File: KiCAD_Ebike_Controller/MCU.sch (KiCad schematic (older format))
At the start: 16 parts, among them SW1 SW_Push, U1 STM32F030K6Tx, Y1 Crystal_GND2_Small

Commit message: 50% of the way through the layout
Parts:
- removed R20: 100k, symbol Device:R_Small
- removed Y1: Crystal_GND2_Small, symbol Device:Crystal_GND2_Small
- added C33, C34: 100n, Capacitor_SMD:C_0805_2012Metric_Pad1.15x1.40mm_HandSolder, symbol Device:C_Small
- added Y1: Crystal, Crystal:Crystal_SMD_HC49-SD, symbol Device:Crystal
- C5: value 10n -> 100n; footprint Capacitor_SMD:C_0603_1608Metric_Pad1.05x0.95mm_HandSolder -> Capacitor_SMD:C_0805_2012Metric_Pad1.15x1.40mm_HandSolder
- C6, C7, C8: footprint Capacitor_SMD:C_0805_2012Metric -> Capacitor_SMD:C_0805_2012Metric_Pad1.15x1.40mm_HandSolder
- R16, R17, R18, R19: footprint (none) -> Resistor_SMD:R_0805_2012Metric_Pad1.15x1.40mm_HandSolder
- SW1: footprint (none) -> Button_Switch_SMD:SW_Push_1P1T_NO_6x6mm_H9.5mm
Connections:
- net labels added: GNDA
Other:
- moved on the sheet: C8
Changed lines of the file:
@@
 SPI1_NSS
-$Comp
-L Device:Crystal_GND2_Small Y1
-U 1 1 5F915CDC
-P 4800 3650
-F 0 "Y1" V 4800 3750 50  0000 L CNN
-F 1 "Crystal_GND2_Small" V 4800 2650 50  0001 L CNN
-F 2 "" H 4800 3650 50  0001 C CNN
-F 3 "~" H 4800 3650 50  0001 C CNN
-	1    4800 3650
-	0    1    1    0
-$EndComp
 $Comp
 L Device:C_Small C11
@@
 $EndComp
 Wire Wire Line
-	4800 3550 4800 3500
-Wire Wire Line
-	4800 3500 4650 3500
-Wire Wire Line
-	4800 3750 4800 3800
-Wire Wire Line
-	4800 3800 4650 3800
-Wire Wire Line
-	4400 3800 4400 3650
-Wire Wire Line
 	4400 3500 4450 3500
 Wire Wire Line
-	4700 3650 4400 3650
-Connection ~ 4400 3650
-Wire Wire Line
-	4400 3650 4400 3500
-Wire Wire Line
-	5000 3500 4800 3500
-Wire Wire Line
 	5000 3500 5000 3600
-Connection ~ 4800 3500
-Wire Wire Line
-	4800 3800 5000 3800
 Wire Wire Line
 	5000 3700 5000 3800
-Connection ~ 4800 3800
 $Comp
 L Device:C_Small C10
@@
 	7850 4500 6100 4500
 Wire Wire Line
-	5000 4100 3450 4100
+	5000 4100 3400 4100
 Text HLabel 2550 3900 0    50   Input ~ 0
 HALL_A_PB0
@@
 Wire Wire Line
 	6100 4400 7850 4400
-Wire Wire Line
-	5000 3000 4650 3000
 Text HLabel 2550 3000 0    50   Input ~ 0
 nRST
-$Comp
-L Device:R_Small R20
-U 1 1 5F9AB9AE
-P 4650 2850
-F 0 "R20" H 4709 2896 50  0000 L CNN
-F 1 "100k" H 4709 2805 50  0000 L CNN
-F 2 "" H 4650 2850 50  0001 C CNN
-F 3 "~" H 4650 2850 50  0001 C CNN
-	1    4650 2850
-	1    0    0    -1
-$EndComp
 Connection ~ 3950 3000
 Wire Wire Line
 	3950 3000 3950 3100
-Wire Wire Line
-	4650 2750 4650 2700
-Wire Wire Line
-	4650 2700 5500 2700
-Connection ~ 5500 2700
 $Comp
 L Device:C_Small C9
@@
 Wire Wire Line
 	3950 3000 3700 3000
-Wire Wire Line
-	4650 2950 4650 3000
-Connection ~ 4650 3000
-Wire Wire Line
-	4650 3000 3950 3000
 $Comp
 L Switch:SW_Push SW1
@@
 F 0 "SW1" V 3654 3202 50  0000 R CNN
 F 1 "SW_Push" V 3745 3202 50  0000 R CNN
-F 2 "" H 3700 3450 50  0001 C CNN
+F 2 "Button_Switch_SMD:SW_Push_1P1T_NO_6x6mm_H9.5mm" H 3700 3450 50  0001 C CNN
 F 3 "~" H 3700 3450 50  0001 C CNN
 	1    3700 3250
@@
 F 0 "R19" H 4359 3346 50  0000 L CNN
 F 1 "100k" H 4359 3255 50  0000 L CNN
-F 2 "" H 4300 3300 50  0001 C CNN
+F 2 "Resistor_SMD:R_0805_2012Metric_Pad1.15x1.40mm_HandSolder" H 4300 3300 50  0001 C CNN
 F 3 "~" H 4300 3300 50  0001 C CNN
 	1    4300 3300
@@
 F 0 "R16" H 2759 3746 50  0000 L CNN
 F 1 "100k" H 2759 3655 50  0000 L CNN
-F 2 "" H 2700 3700 50  0001 C CNN
+F 2 "Resistor_SMD:R_0805_2012Metric_Pad1.15x1.40mm_HandSolder" H 2700 3700 50  0001 C CNN
 F 3 "~" H 2700 3700 50  0001 C CNN
 	1    2700 3700
@@
 F 0 "R17" H 3059 3746 50  0000 L CNN
 F 1 "100k" H 3059 3655 50  0000 L CNN
-F 2 "" H 3000 3700 50  0001 C CNN
+F 2 "Resistor_SMD:R_0805_2012Metric_Pad1.15x1.40mm_HandSolder" H 3000 3700 50  0001 C CNN
 F 3 "~" H 3000 3700 50  0001 C CNN
 	1    3000 3700
@@
 F 0 "R18" H 3359 3746 50  0000 L CNN
 F 1 "100k" H 3359 3655 50  0000 L CNN
-F 2 "" H 3300 3700 50  0001 C CNN
+F 2 "Resistor_SMD:R_0805_2012Metric_Pad1.15x1.40mm_HandSolder" H 3300 3700 50  0001 C CNN
 F 3 "~" H 3300 3700 50  0001 C CNN
 	1    3300 3700
@@
 Text HLabel 1600 1950 0    50   Input ~ 0
 +3.3v
-$Comp
-L power:GND #PWR0110
-U 1 1 5FABED44
-P 1950 2600
-F 0 "#PWR0110" H 1950 2350 50  0001 C CNN
-F 1 "GND" H 1955 2427 50  0000 C CNN
-F 2 "" H 1950 2600 50  0001 C CNN
-F 3 "" H 1950 2600 50  0001 C CNN
-	1    1950 2600
-	1    0    0    -1
-$EndComp
-$Comp
-L power:GND #PWR0111
-U 1 1 5FACF53C
-P 3700 3650
-F 0 "#PWR0111" H 3700 3400 50  0001 C CNN
-F 1 "GND" H 3705 3477 50  0000 C CNN
-F 2 "" H 3700 3650 50  0001 C CNN
-F 3 "" H 3700 3650 50  0001 C CNN
-	1    3700 3650
-	1    0    0    -1
-$EndComp
-$Comp
-L power:GND #PWR0112
-U 1 1 5FACFE3C
-P 5500 4950
-F 0 "#PWR0112" H 5500 4700 50  0001 C CNN
-F 1 "GND" H 5505 4777 50  0000 C CNN
-F 2 "" H 5500 4950 50  0001 C CNN
-F 3 "" H 5500 4950 50  0001 C CNN
-	1    5500 4950
-	1    0    0    -1
-$EndComp
 Wire Wire Line
 	1600 2300 1950 2300
@@
 Text Notes 6200 3200 0    50   ~ 0
 ADC_IN2
-Text HLabel 7850 3200 2    50   Input ~ 0
-THROTTLE_PA2
-Wire Wire Line
-	6100 3200 7850 3200
 Wire Wire Line
 	7100 3800 7100 3850
@@
 F 0 "C6" H 2892 4796 50  0000 L CNN
 F 1 "100n" H 2892 4705 50  0000 L CNN
-F 2 "Capacitor_SMD:C_0805_2012Metric" H 2800 4750 50  0001 C CNN
+F 2 "Capacitor_SMD:C_0805_2012Metric_Pad1.15x1.40mm_HandSolder" H 2800 4750 50  0001 C CNN
 F 3 "~" H 2800 4750 50  0001 C CNN
 	1    2800 4750
@@
 F 0 "C7" H 3192 4796 50  0000 L CNN
 F 1 "100n" H 3192 4705 50  0000 L CNN
-F 2 "Capacitor_SMD:C_0805_2012Metric" H 3100 4750 50  0001 C CNN
+F 2 "Capacitor_SMD:C_0805_2012Metric_Pad1.15x1.40mm_HandSolder" H 3100 4750 50  0001 C CNN
 F 3 "~" H 3100 4750 50  0001 C CNN
 	1    3100 4750
@@
 L Device:C_Small C8
 U 1 1 5FCC70C3
-P 3450 4750
-F 0 "C8" H 3542 4796 50  0000 L CNN
-F 1 "100n" H 3542 4705 50  0000 L CNN
-F 2 "Capacitor_SMD:C_0805_2012Metric" H 3450 4750 50  0001 C CNN
-F 3 "~" H 3450 4750 50  0001 C CNN
-	1    3450 4750
+P 3400 4750
+F 0 "C8" H 3492 4796 50  0000 L CNN
+F 1 "100n" H 3492 4705 50  0000 L CNN
+F 2 "Capacitor_SMD:C_0805_2012Metric_Pad1.15x1.40mm_HandSolder" H 3400 4750 50  0001 C CNN
+F 3 "~" H 3400 4750 50  0001 C CNN
+	1    3400 4750
 	1    0    0    -1
 $EndComp
@@
 	3100 4000 5000 4000
 Wire Wire Line
-	3450 4100 3450 4650
-Connection ~ 3450 4100
-Wire Wire Line
-	3450 4100 3300 4100
+	3400 4100 3400 4650
+Connection ~ 3400 4100
+Wire Wire Line
+	3400 4100 3300 4100
 Wire Wire Line
 	2800 4850 2800 5000
@@
 	2800 5000 3100 5000
 Wire Wire Line
-	3450 5000 3450 4850
+	3400 5000 3400 4850
 Wire Wire Line
 	3100 4850 3100 5000
 Connection ~ 3100 5000
-$Comp
-L power:GND #PWR0113
-U 1 1 5FCE6083
-P 3200 5150
-F 0 "#PWR0113" H 3200 4900 50  0001 C CNN
-F 1 "GND" H 3205 4977 50  0000 C CNN
-F 2 "" H 3200 5150 50  0001 C CNN
-F 3 "" H 3200 5150 50  0001 C CNN
-	1    3200 5150
-	1    0    0    -1
-$EndComp
 Wire Wire Line
 	3100 5000 3200 5000
@@
 Connection ~ 3200 5000
 Wire Wire Line
-	3200 5000 3450 5000
+	3200 5000 3400 5000
 $Comp
 L Device:C_Small C5
@@
 P 2450 2150
 F 0 "C5" H 2542 2196 50  0000 L CNN
-F 1 "10n" H 2542 2105 50  0000 L CNN
-F 2 "Capacitor_SMD:C_0603_1608Metric_Pad1.05x0.95mm_HandSolder" H 2450 2150 50  0001 C CNN
+F 1 "100n" H 2542 2105 50  0000 L CNN
+F 2 "Capacitor_SMD:C_0805_2012Metric_Pad1.15x1.40mm_HandSolder" H 2450 2150 50  0001 C CNN
 F 3 "~" H 2450 2150 50  0001 C CNN
 	1    2450 2150
@@
 Wire Wire Line
 	2450 2300 2100 2300
+Connection ~ 2100 2300
+Wire Wire Line
+	3950 3000 5000 3000
+$Comp
+L power:GNDA #PWR0113
+U 1 1 5FEA90DB
+P 5500 4950
+F 0 "#PWR0113" H 5500 4700 50  0001 C CNN
+F 1 "GNDA" H 5505 4777 50  0000 C CNN
+F 2 "" H 5500 4950 50  0001 C CNN
+F 3 "" H 5500 4950 50  0001 C CNN
+	1    5500 4950
+	1    0    0    -1
+$EndComp
+$Comp
+L power:GNDA #PWR0116
+U 1 1 5FEAA964
+P 3700 3650
+F 0 "#PWR0116" H 3700 3400 50  0001 C CNN
+F 1 "GNDA" H 3705 3477 50  0000 C CNN
+F 2 "" H 3700 3650 50  0001 C CNN
+F 3 "" H 3700 3650 50  0001 C CNN
+	1    3700 3650
+	1    0    0    -1
+$EndComp
+$Comp
+L power:GNDA #PWR0122
+U 1 1 5FEAF53C
+P 3200 5150
+F 0 "#PWR0122" H 3200 4900 50  0001 C CNN
+F 1 "GNDA" H 3205 4977 50  0000 C CNN
+F 2 "" H 3200 5150 50  0001 C CNN
+F 3 "" H 3200 5150 50  0001 C CNN
+	1    3200 5150
+	1    0    0    -1
+$EndComp
+$Comp
+L power:GNDA #PWR0123
+U 1 1 5FEB4CC6
+P 1950 2600
+F 0 "#PWR0123" H 1950 2350 50  0001 C CNN
+F 1 "GNDA" H 1955 2427 50  0000 C CNN
+F 2 "" H 1950 2600 50  0001 C CNN
+F 3 "" H 1950 2600 50  0001 C CNN
+	1    1950 2600
+	1    0    0    -1
+$EndComp
+Wire Wire Line
+	4400 3500 4400 3800
+Wire Wire Line
+	5000 3500 4800 3500
+Connection ~ 4800 3500
+Wire Wire Line
+	4650 3500 4800 3500
+Connection ~ 4800 3800
+Wire Wire Line
+	4800 3800 5000 3800
+Wire Wire Line
+	4650 3800 4800 3800
+$Comp
+L Device:Crystal Y1
+U 1 1 5FF5B830
+P 4800 3650
+F 0 "Y1" V 4600 3650 50  0000 L CNN
+F 1 "Crystal" V 4500 3650 50  0000 L CNN
+F 2 "Crystal:Crystal_SMD_HC49-SD" H 4800 3650 50  0001 C CNN
+F 3 "~" H 4800 3650 50  0001 C CNN
+	1    4800 3650
+	0    1    1    0
+$EndComp
+Text HLabel 7850 3200 2    50   Input ~ 0
+THROTTLE_PA2
+Wire Wire Line
+	6100 3200 7850 3200
+$Comp
+L Device:C_Small C33
+U 1 1 60096170
+P 2850 2150
+F 0 "C33" H 2942 2196 50  0000 L CNN
+F 1 "100n" H 2942 2105 50  0000 L CNN
+F 2 "Capacitor_SMD:C_0805_2012Metric_Pad1.15x1.40mm_HandSolder" H 2850 2150 50  0001 C CNN
+F 3 "~" H 2850 2150 50  0001 C CNN
+	1    2850 2150
+	1    0    0    -1
+$EndComp
+Wire Wire Line
+	2450 1950 2850 1950
+Wire Wire Line
+	2850 1950 2850 2050
+Connection ~ 2450 1950
+Wire Wire Line
+	2850 2250 2850 2300
+Wire Wire Line
+	2850 2300 2450 2300
+Connection ~ 2450 2300
+$Comp
+L Device:C_Small C34
+U 1 1 6009E0FA
+P 3250 2150
+F 0 "C34" H 3342 2196 50  0000 L CNN
+F 1 "100n" H 3342 2105 50  0000 L CNN
+F 2 "Capacitor_SMD:C_0805_2012Metric_Pad1.15x1.40mm_HandSolder" H 3250 2150 50  0001 C CNN
+F 3 "~" H 3250 2150 50  0001 C CNN
+	1    3250 2150
+	1    0    0    -1
+$EndComp
+Wire Wire Line
+	2850 1950 3250 1950
+Wire Wire Line
+	3250 1950 3250 2050
+Connection ~ 2850 1950
+Wire Wire Line
+	3250 2250 3250 2300
+Wire Wire Line
+	3250 2300 2850 2300
+Connection ~ 2850 2300
 Wire Bus Line
 	7200 3900 7200 4100
 Wire Bus Line
 	7150 3500 7150 3800
-Connection ~ 2100 2300
 $EndSCHEMATC

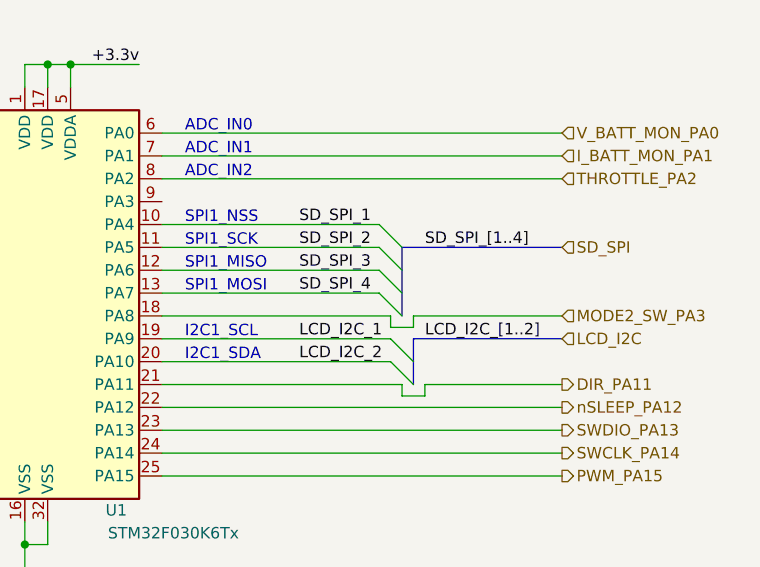
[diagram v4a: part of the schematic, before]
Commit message: Layout done. will tidy up ref des next
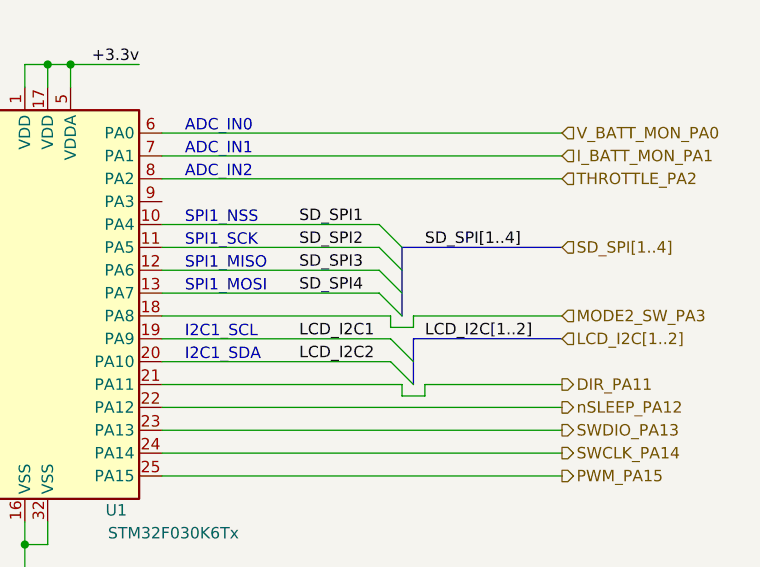
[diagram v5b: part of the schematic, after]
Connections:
- net LCD_I2C_1 renamed LCD_I2C1
- net LCD_I2C_2 renamed LCD_I2C2
- net SD_SPI_1 renamed SD_SPI1
- net SD_SPI_2 renamed SD_SPI2
- net SD_SPI_3 renamed SD_SPI3
- net SD_SPI_4 renamed SD_SPI4
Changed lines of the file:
@@
 $Descr A4 11693 8268
 encoding utf-8
-Sheet 3 7
+Sheet 7 7
 Title ""
 Date ""
@@
 Text HLabel 1600 2300 0    50   Input ~ 0
 GND
-Text HLabel 7850 4500 2    50   Output ~ 0
-PWM_PA15
-Text HLabel 7850 4100 2    50   Output ~ 0
-DIR_PA11
-Text HLabel 7850 4200 2    50   Output ~ 0
-nSLEEP_PA12
 Wire Wire Line
 	6100 3000 7850 3000
@@
 Text Notes 6200 3900 0    50   ~ 0
 I2C1_SCL
-Wire Wire Line
-	7050 3700 6100 3700
 Wire Wire Line
 	6100 3600 7050 3600
@@
 MODE2_SW_PA3
 Text HLabel 7850 3500 2    50   Input ~ 0
-SD_SPI
-Text HLabel 7850 3900 2    50   Input ~ 0
-LCD_I2C
+SD_SPI[1..4]
 Wire Bus Line
 	7150 3500 7850 3500
@@
 	7050 3700 7150 3800
 Text Label 6700 3400 0    50   ~ 0
-SD_SPI_1
+SD_SPI1
 Text Label 6700 3500 0    50   ~ 0
-SD_SPI_2
+SD_SPI2
 Text Label 6700 3600 0    50   ~ 0
-SD_SPI_3
+SD_SPI3
 Text Label 6700 3700 0    50   ~ 0
-SD_SPI_4
+SD_SPI4
 Text Label 7250 3500 0    50   ~ 0
-SD_SPI_[1..4]
+SD_SPI[1..4]
 Text Label 6700 3900 0    50   ~ 0
-LCD_I2C_1
+LCD_I2C1
 Text Label 6700 4000 0    50   ~ 0
-LCD_I2C_2
+LCD_I2C2
 Wire Bus Line
 	7850 3900 7200 3900
 Entry Wire Line
-	7100 4000 7200 4100
-Wire Wire Line
-	6100 4000 7100 4000
-Entry Wire Line
 	7100 3900 7200 4000
 Wire Wire Line
 	6100 3900 7100 3900
-Wire Wire Line
-	7250 4150 7250 4100
-Wire Wire Line
-	7250 4100 7850 4100
-Wire Wire Line
-	7850 4200 6100 4200
-Wire Wire Line
-	7250 4150 7150 4150
-Wire Wire Line
-	7150 4150 7150 4100
-Wire Wire Line
-	7150 4100 6100 4100
 Text Label 7250 3900 0    50   ~ 0
-LCD_I2C_[1..2]
-Wire Wire Line
-	7850 4500 6100 4500
+LCD_I2C[1..2]
 Wire Wire Line
 	5000 4100 3400 4100
@@
 Wire Wire Line
 	5000 4200 2550 4200
-Wire Wire Line
-	6100 4300 7850 4300
-Text HLabel 7850 4300 2    50   Output ~ 0
-SWDIO_PA13
-Text HLabel 7850 4400 2    50   Output ~ 0
-SWCLK_PA14
-Wire Wire Line
-	6100 4400 7850 4400
 Text HLabel 2550 3000 0    50   Input ~ 0
 nRST
@@
 	3250 2300 2850 2300
 Connection ~ 2850 2300
+Wire Wire Line
+	6100 3700 7050 3700
+Entry Wire Line
+	7100 4000 7200 4100
+Wire Wire Line
+	6100 4000 7100 4000
+Text HLabel 7850 3900 2    50   Input ~ 0
+LCD_I2C[1..2]
+Wire Wire Line
+	6100 4400 7850 4400
+Text HLabel 7850 4400 2    50   Output ~ 0
+SWCLK_PA14
+Text HLabel 7850 4300 2    50   Output ~ 0
+SWDIO_PA13
+Wire Wire Line
+	6100 4300 7850 4300
+Wire Wire Line
+	7850 4500 6100 4500
+Wire Wire Line
+	7150 4100 6100 4100
+Wire Wire Line
+	7150 4150 7150 4100
+Wire Wire Line
+	7250 4150 7150 4150
+Wire Wire Line
+	7850 4200 6100 4200
+Wire Wire Line
+	7250 4100 7850 4100
+Wire Wire Line
+	7250 4150 7250 4100
+Text HLabel 7850 4200 2    50   Output ~ 0
+nSLEEP_PA12
+Text HLabel 7850 4100 2    50   Output ~ 0
+DIR_PA11
+Text HLabel 7850 4500 2    50   Output ~ 0
+PWM_PA15
 Wire Bus Line
 	7200 3900 7200 4100
